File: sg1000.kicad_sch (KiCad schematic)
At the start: 71 parts, among them CN1 Conn_01x07_Female, J1 USB-B1HSB6, J2 RCJ-014, J3 RCJ-013, Q1 2n4401, Q1c1 2n3906, SW1 Pause Key, SW2 Power Toggle, SW3 Reset Key, U1 SG-1000-Cart, U100 74HCT574, U101 74HCT574, U102 74HCT574, U103 AS6C62256-DIP, U11 AS6C62256-DIP, U12 TMS9918A, U13 74LS139, U16 74LS32, U18 74LS257, U2 SG-1000-Expansion, U21 74LS257, U3 SN76489AN, U4 74LS32, U5 27C256, U6 74LS573, U7 74LS00, U9 Z80CPU, U99 74HCT04, X2 10.73863MHz

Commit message: Add JOY_SEL to edge
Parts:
- U103, U11: footprint Package_DIP:DIP-28_W15.24mm_Socket_LongPads -> Housings_DIP:DIP-28_W15.24mm_Socket_LongPads
- U12: footprint Package_DIP:DIP-40_W15.24mm_Socket_LongPads -> Housings_DIP:DIP-40_W15.24mm_Socket_LongPads
- U5: footprint Socket:DIP_Socket-28_W11.9_W12.7_W15.24_W17.78_W18.5_3M_228-1277-00-0602J -> Package_DIP:DIP-28_W15.24mm
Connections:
- net GND: no longer J1.P1 (S1), J1.P2 (S2)
- net ~{JOY_SEL}: now also U2.3 (~{JOY_SEL})
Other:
- note added: "June 2022: ~{JOY_SEL} wired to pin 3"
- note added: "TODO: Needs confirmation"
- note removed: "TODO: ~{JOYSEL} is missing!"

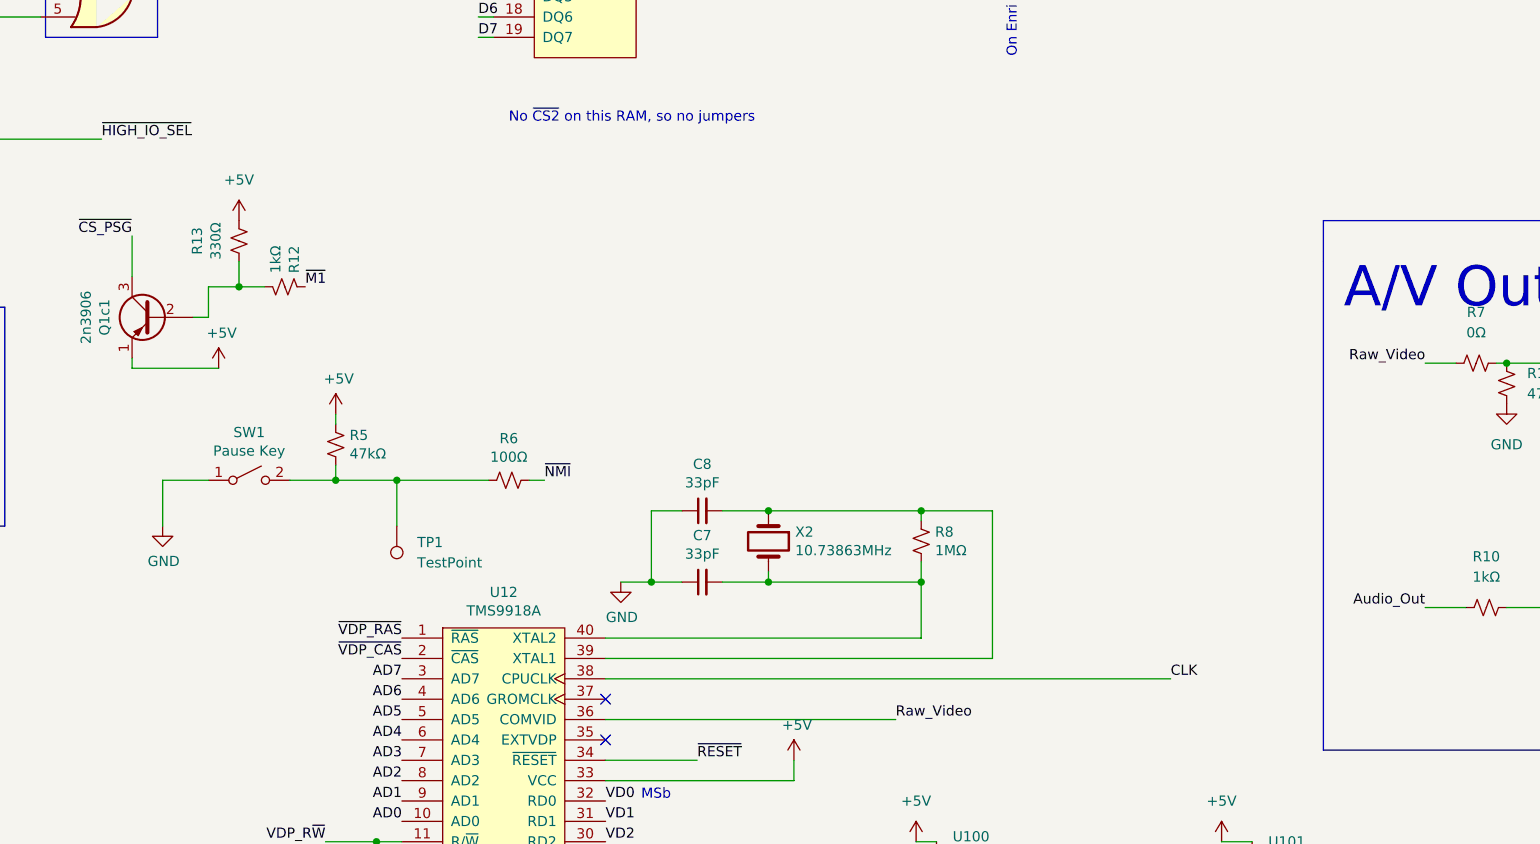
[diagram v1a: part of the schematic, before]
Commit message: Stolen MiniPET debounce circuit for /NMI
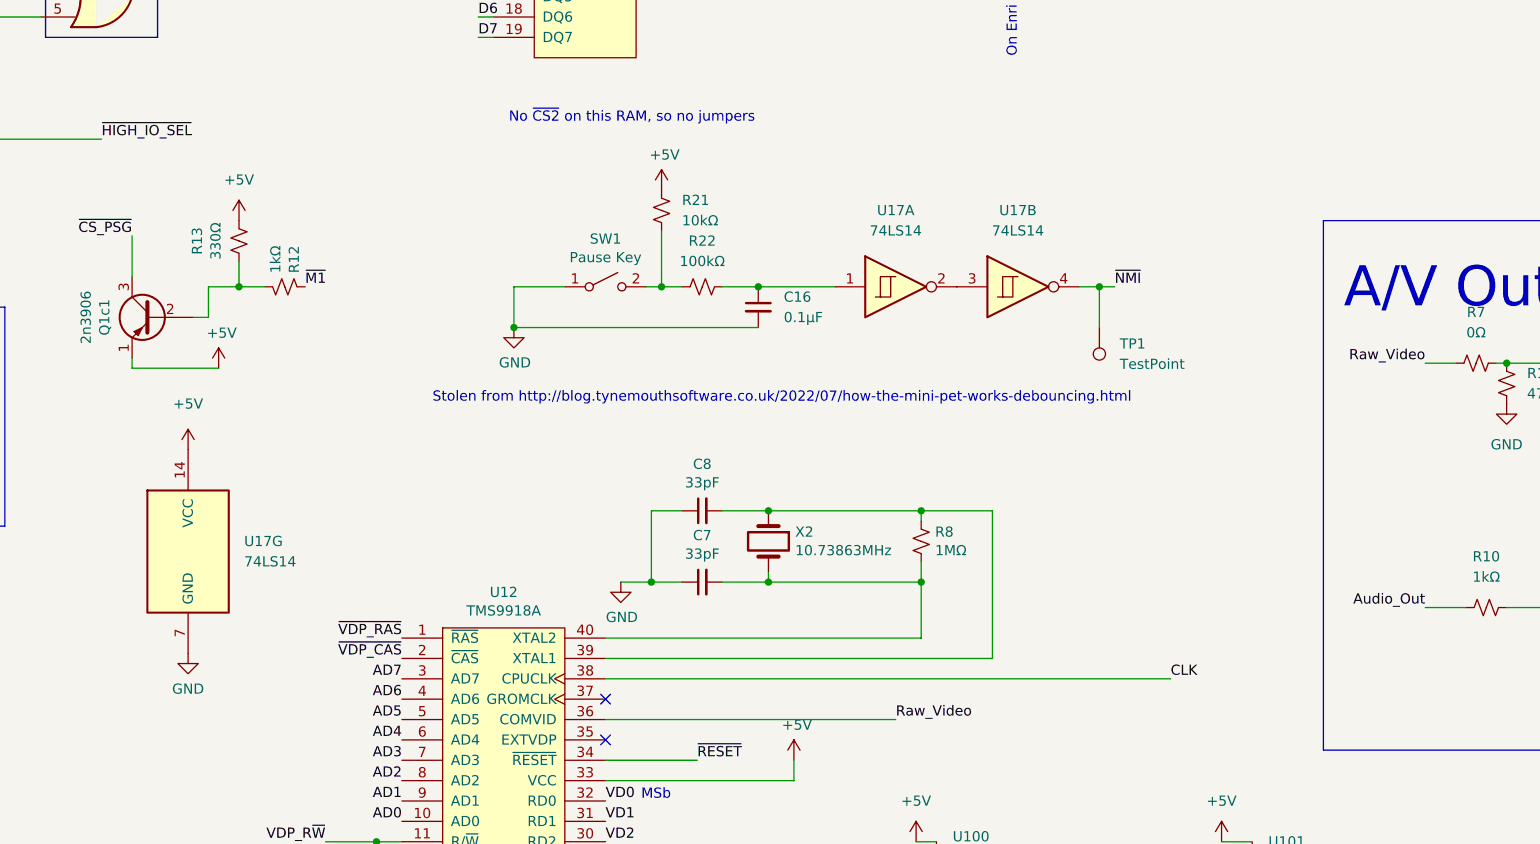
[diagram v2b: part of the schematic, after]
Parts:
- removed R5: 47kΩ, Resistor_SMD:R_0805_2012Metric_Pad1.15x1.40mm_HandSolder, symbol Device:R_Small_US
- removed R6: 100Ω, Resistor_SMD:R_0805_2012Metric_Pad1.15x1.40mm_HandSolder, symbol Device:R_Small_US
- added C16: 0.1µF, Capacitor_SMD:C_0805_2012Metric_Pad1.18x1.45mm_HandSolder, symbol Device:C_Small
- added R21: 10kΩ, Resistor_SMD:R_0805_2012Metric_Pad1.20x1.40mm_HandSolder, symbol Device:R_Small_US
- added R22: 100kΩ, Resistor_SMD:R_0805_2012Metric_Pad1.20x1.40mm_HandSolder, symbol Device:R_Small_US
- added U17: 74LS14, Package_DIP:DIP-14_W7.62mm_Socket_LongPads, symbol 74xx:74LS14
- U103, U11: footprint Housings_DIP:DIP-28_W15.24mm_Socket_LongPads -> Package_DIP:DIP-28_W15.24mm_Socket_LongPads
- U12: footprint Housings_DIP:DIP-40_W15.24mm_Socket_LongPads -> Package_DIP:DIP-40_W15.24mm_Socket_LongPads
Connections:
- net +5V: now also R21.1, U17.14 (VCC)
- net GND: now also C16.2, U17.7 (GND)
- net ~{NMI}: now also TP1.1, U17.4
- net at SW1.2 (B): now also R21.2, R22.1; no longer TP1.1
- new net: U17.2, U17.3
- new net: C16.1, R22.2, U17.1
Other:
- note added: "Stolen from http://blog.tynemouthsoftware.co.uk/2022/07/how-the-mini-pet-works-debouncing.html"
- moved on the sheet: SW1, TP1

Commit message: Keyboard detection in ramtest
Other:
- note removed: "TODO: Needs confirmation"
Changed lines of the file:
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@@
     (effects (font (size 5.0038 5.0038)) (justify left bottom))
-  )
-  (text "TODO: Needs confirmation" (at 193.04 554.99 180)
-    (effects (font (size 1.27 1.27)) (justify right bottom))
   )
   (text "CSCN4 = Mark III only, and it seems to\nbe shorted to B1 on real SG-1000 carts,\nso we're going to use this signal for\ncartridge detection."

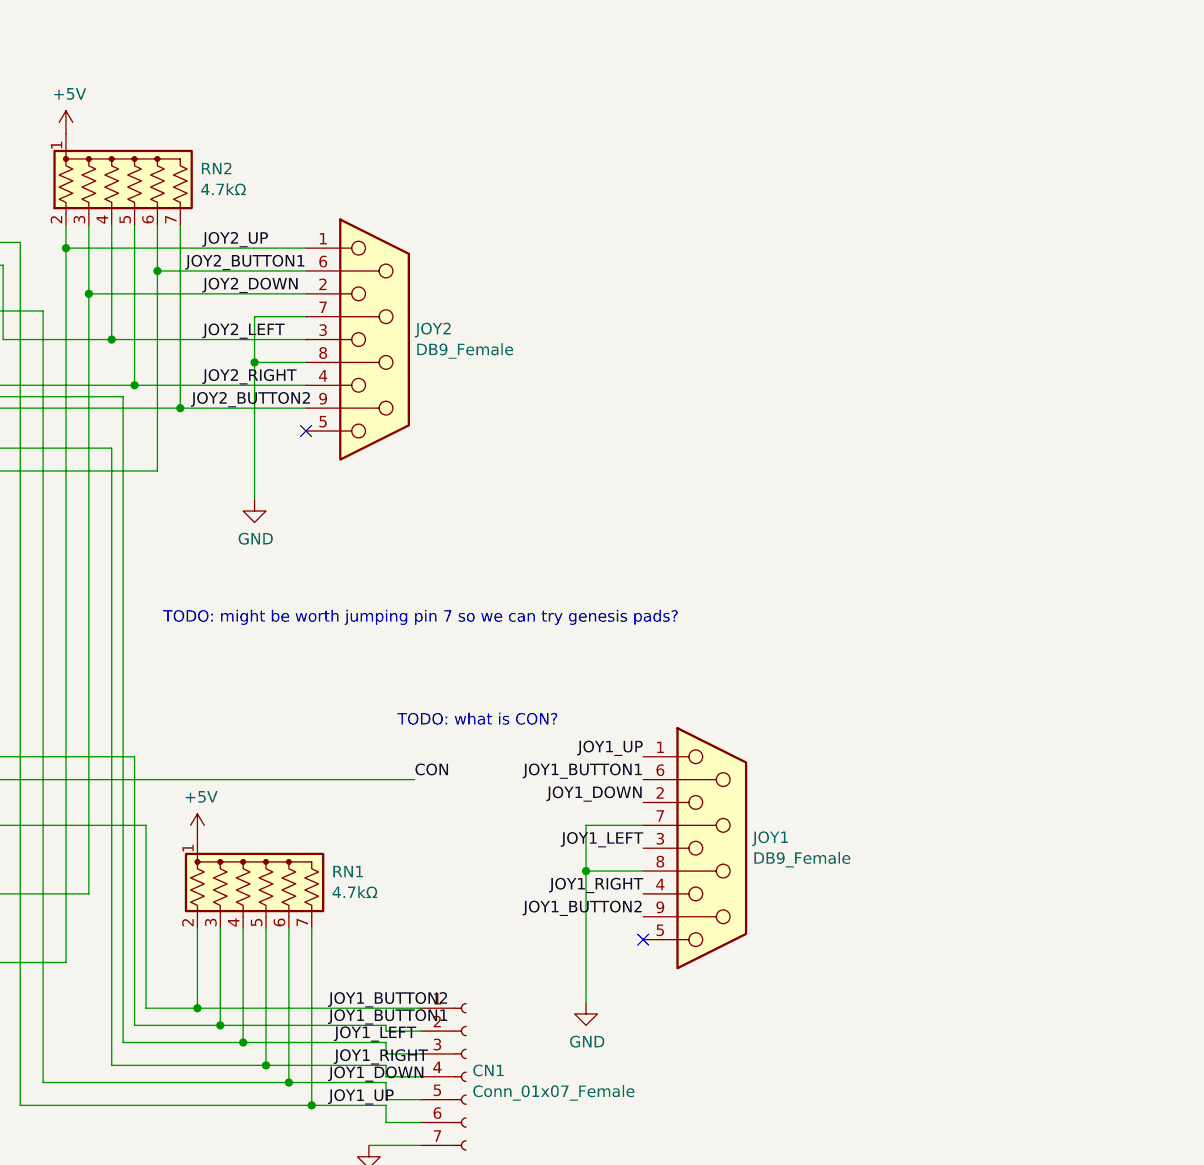
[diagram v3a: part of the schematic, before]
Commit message: Add power to controller for MD controllers
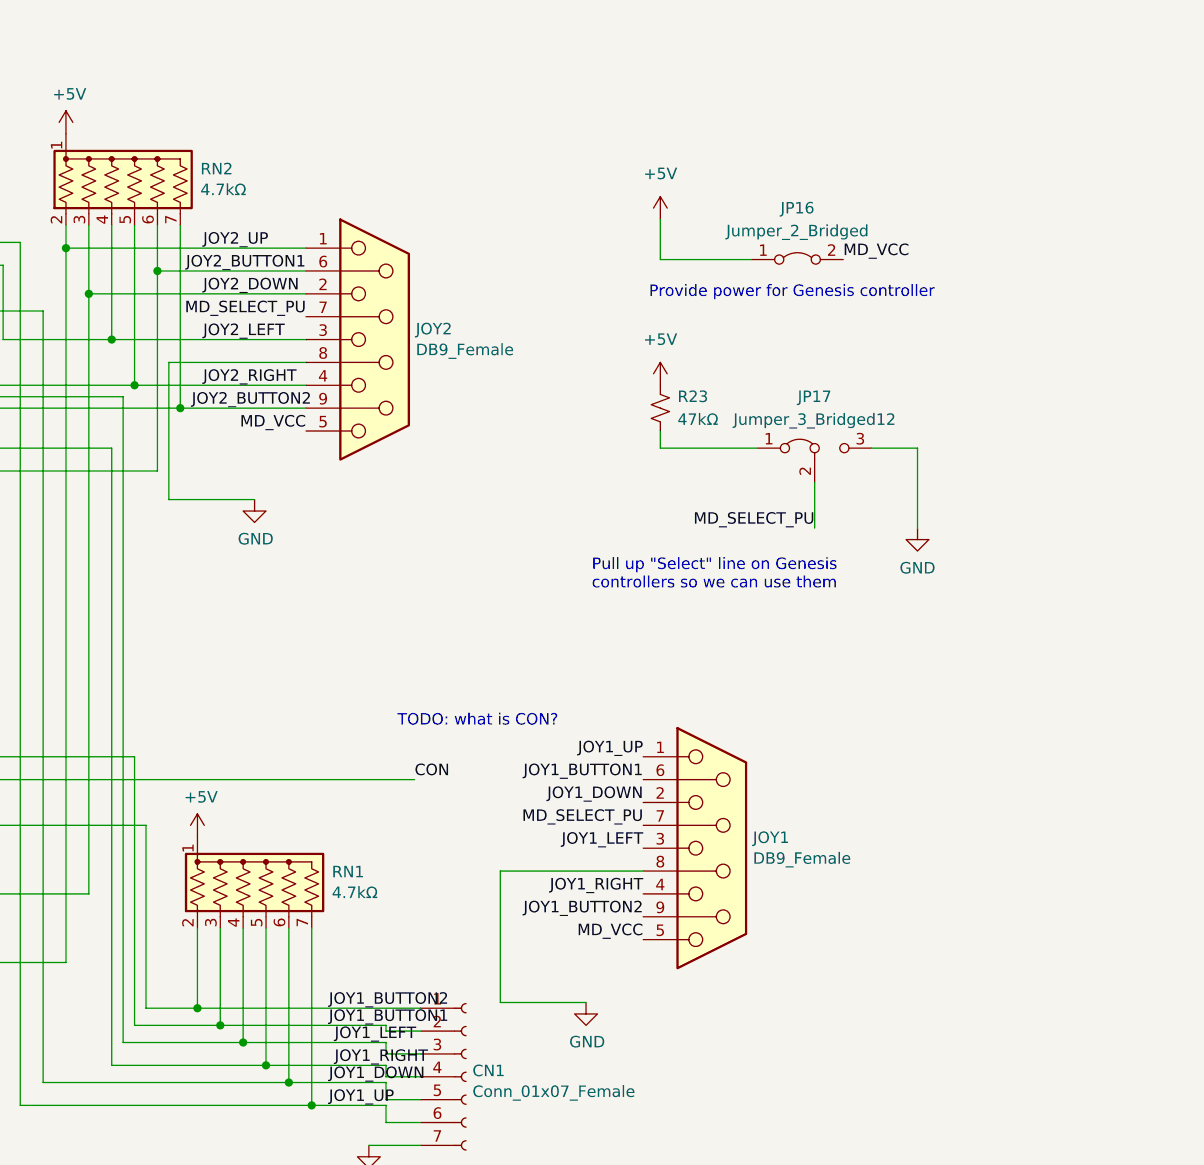
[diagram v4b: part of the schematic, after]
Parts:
- added JP16: Jumper_2_Bridged, Jumper:SolderJumper-2_P1.3mm_Bridged_Pad1.0x1.5mm, symbol Jumper:Jumper_2_Bridged
- added JP17: Jumper_3_Bridged12, Jumper:SolderJumper-3_P1.3mm_Bridged2Bar12_Pad1.0x1.5mm_NumberLabels, symbol Jumper:Jumper_3_Bridged12
- added R23: 47kΩ, Resistor_SMD:R_0805_2012Metric_Pad1.20x1.40mm_HandSolder, symbol Device:R_Small_US
- J1: footprint OST_USB-B1HSB6 -> USB-B1HSB6:OST_USB-B1HSB6
- J2, J3: footprint CUI_RCJ-017 -> Jacks:CUI_RCJ-017
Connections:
- net +5V: now also JP16.1 (A), R23.1
- net GND: now also JP17.3 (B); no longer JOY1.7, JOY2.7
- net MD_VCC: now reaches JOY2.5
- net MD_VCC: now also JOY1.5, JP16.2 (B)
- new net: JP17.1 (A), R23.2
- new net MD_SELECT_PU: JOY1.7, JOY2.7, JP17.2 (C)
- no-connect marks 27 -> 25
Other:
- note added: "Provide power for Genesis controller"
- note added: "Pull up "Select" line on Genesis controllers so we can use them"
- note removed: "TODO: might be worth jumping pin 7 so we can try genesis pads?"
